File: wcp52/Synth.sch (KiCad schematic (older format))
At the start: 52 parts, among them U3 LMH6714MF, U4 AD9958BCPZ, U5 LMH6714MF, X1 25 MHz

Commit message: Reorganize MPU schematic
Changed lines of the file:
@@
 Text HLabel 1350 4800 0    60   Input ~ 0
 SDI
-Text HLabel 1350 4900 0    60   Input ~ 0
+Text HLabel 1350 4900 0    60   BiDi ~ 0
 SDIO_1
 Text HLabel 1350 5000 0    60   Output ~ 0

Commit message: Reannotate parts. May need to tweak silkscreen
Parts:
- C10: renamed from C6; OldReference (none) -> C6
- C11: renamed from C14; OldReference (none) -> C14
- C12: renamed from C7; OldReference (none) -> C7
- C13: renamed from C15; OldReference (none) -> C15
- C14: renamed from C11; OldReference (none) -> C11
- C15: renamed from C12; OldReference (none) -> C12
- C16: renamed from C8; OldReference (none) -> C8
- C17: renamed from C16; OldReference (none) -> C16
- C18: renamed from C9; OldReference (none) -> C9
- C19: renamed from C17; OldReference (none) -> C17
- C20: renamed from C10; OldReference (none) -> C10
- C21: renamed from C19; OldReference (none) -> C19
- C22: renamed from C20; OldReference (none) -> C20
- C23: renamed from C21; OldReference (none) -> C21
- C24: renamed from C22; OldReference (none) -> C22
- C25: renamed from C23; OldReference (none) -> C23
- C26: renamed from C24; OldReference (none) -> C24
- C27: renamed from C25; OldReference (none) -> C25
- C28: renamed from C26; OldReference (none) -> C26
- C29: renamed from C27; OldReference (none) -> C27
- C30: renamed from C18; OldReference (none) -> C18
- C31: renamed from C55; OldReference (none) -> C55
- C8: renamed from C5; OldReference (none) -> C5
- C9: renamed from C13; OldReference (none) -> C13
- E2: OldReference (none) -> E2
- R18: renamed from R13; OldReference (none) -> R13
- R19: renamed from R14; OldReference (none) -> R14
- R20: renamed from R12; OldReference (none) -> R12
- R21: renamed from R15; OldReference (none) -> R15
- R22: renamed from R17; OldReference (none) -> R17
- R23: renamed from R18; OldReference (none) -> R18
- R24: renamed from R19; OldReference (none) -> R19
- R25: renamed from R20; OldReference (none) -> R20
- R26: renamed from R21; OldReference (none) -> R21
- R27: renamed from R22; OldReference (none) -> R22
- R28: renamed from R23; OldReference (none) -> R23
- R29: renamed from R24; OldReference (none) -> R24
- R30: renamed from R25; OldReference (none) -> R25
- R31: renamed from R26; OldReference (none) -> R26
- R32: renamed from R27; OldReference (none) -> R27
- R33: renamed from R28; OldReference (none) -> R28
- R34: renamed from R29; OldReference (none) -> R29
- R35: renamed from R30; OldReference (none) -> R30
- R36: renamed from R31; OldReference (none) -> R31
- R37: renamed from R32; OldReference (none) -> R32
- R38: renamed from R33; OldReference (none) -> R33
- R39: renamed from R34; OldReference (none) -> R34
- TP6: renamed from TP2; OldReference (none) -> TP2
- U2: renamed from U3; OldReference (none) -> U3
- U3: renamed from U4; OldReference (none) -> U4
- U4: renamed from U5; OldReference (none) -> U5
- X1: OldReference (none) -> X1
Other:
- note added: "@R20 is copper-bridged on the PCB, it is not necessary to populate a jumper.\nIf this part must be changed after testing, cut the bridge."
- note removed: "@R12 is copper-bridged on the PCB, it is not necessary to populate a jumper.\nIf this part must be changed after testing, cut the bridge."

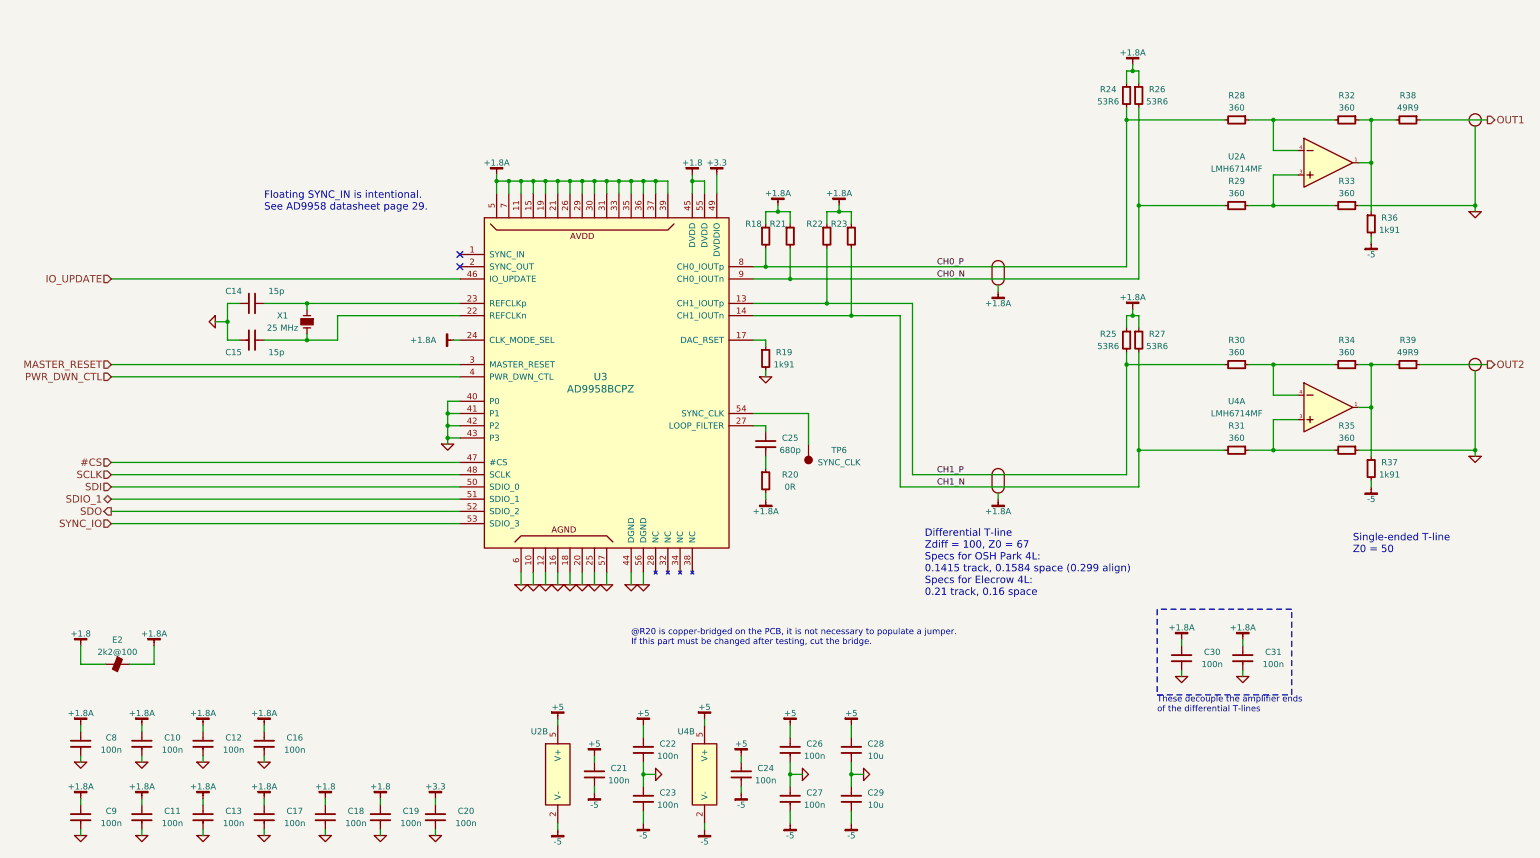
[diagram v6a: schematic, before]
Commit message: Change schematic pages to letter size
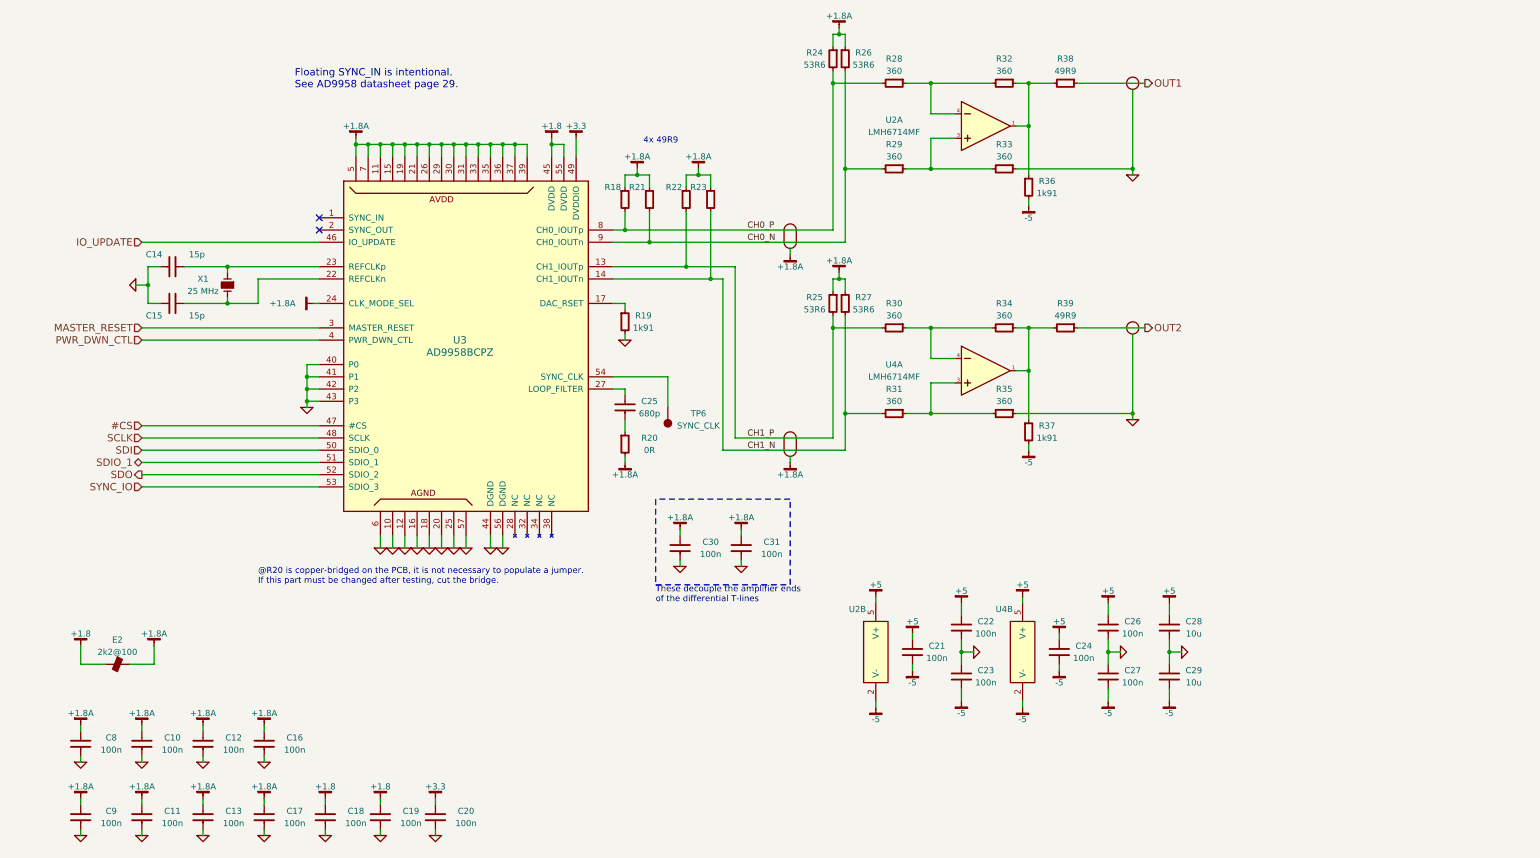
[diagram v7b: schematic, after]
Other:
- note added: "4x 49R9"
- note removed: "Differential T-line\nZdiff = 100, Z0 = 67\nSpecs for OSH Park 4L:\n0.1415 track, 0.1584 space (0.299 align)\nSpecs for Elecrow 4L:\n0.21 track, 0.16 space"
- note removed: "Single-ended T-line\nZ0 = 50"
- moved on the sheet: C14, C15, C21, C22, C23, C24, C25, C26, C27, C28, C29, C30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

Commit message: BOM fixes
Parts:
- U2, U4: BOM DIST DIGIKEY LMH6714MF/NOPBCT-ND -> IC TI LMH6714MF
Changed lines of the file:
@@
 EESchema Schematic File Version 2
-LIBS:Altera
-LIBS:AnalogDevices
-LIBS:Atmel
-LIBS:conn-2mm
-LIBS:conn-100mil
-LIBS:conn-cui
-LIBS:conn-fci
-LIBS:conn-linx
-LIBS:conn-molex
-LIBS:conn-tagconnect
-LIBS:conn-test
-LIBS:DiodesInc
-LIBS:display
-LIBS:_electromech
-LIBS:Fairchild
-LIBS:FTDI
-LIBS:Intersil
-LIBS:Lattice
-LIBS:_linear
-LIBS:LinearTech
-LIBS:Littelfuse
-LIBS:logic-4000
-LIBS:logic-7400
-LIBS:MACOM
-LIBS:maxim
-LIBS:mechanical
-LIBS:Microchip
-LIBS:Micron
-LIBS:NXP
-LIBS:onsemi
-LIBS:passive
-LIBS:pasv-BiTech
-LIBS:pasv-Bourns
-LIBS:pasv-cap
-LIBS:pasv-ind
-LIBS:pasv-res
-LIBS:pcb
-LIBS:power
-LIBS:_semi
-LIBS:semi-diode-1N
-LIBS:semi-diode-BA
-LIBS:semi-diode-MCC
-LIBS:semi-diode-MMB
-LIBS:semi-diode-NXP
-LIBS:semi-diode-OnSemi
-LIBS:semi-diode-Vishay
-LIBS:semi-opto-misc
-LIBS:semi-thyristor-2N
-LIBS:semi-trans-2N
-LIBS:semi-trans-AO
-LIBS:semi-trans-BC
-LIBS:semi-trans-DiodesInc
-LIBS:semi-trans-Fairchild
-LIBS:semi-trans-Infineon
-LIBS:semi-trans-IntRect
-LIBS:semi-trans-IXYS
-LIBS:semi-trans-misc
-LIBS:semi-trans-MMB
-LIBS:semi-trans-MPS
-LIBS:semi-trans-NXP
-LIBS:semi-trans-PZT
-LIBS:semi-trans-TI
-LIBS:semi-trans-TIP
-LIBS:semi-trans-Toshiba
-LIBS:silabs
-LIBS:skyworks
-LIBS:ST
-LIBS:st_ic
-LIBS:st_semi
-LIBS:supertex
-LIBS:symbol
-LIBS:TexasInstruments
-LIBS:vishay_semi
-LIBS:Xilinx
-LIBS:pasv-xtal
-LIBS:conn-te
 LIBS:wcp52-cache
 EELAYER 25 0
@@
 F 2 "smd-semi:SOT-23-5" H 8500 1850 50  0001 C CNN
 F 3 "" H 8300 1850 60  0000 C CNN
-F 4 "DIST DIGIKEY LMH6714MF/NOPBCT-ND" H 9000 2700 60  0001 C CNN "BOM"
-F 5 "Value" H 8500 1850 60  0001 C CNN "Manuf"
+F 4 "Value" H 8500 1850 60  0001 C CNN "Manuf"
+F 5 "IC TI LMH6714MF" H 9000 2700 60  0001 C CNN "BOM"
 F 6 "U3" H 8500 1850 50  0001 C CNN "OldReference"
 	1    8500 1850
@@
 F 2 "smd-semi:SOT-23-5" H 8500 3850 50  0001 C CNN
 F 3 "" H 8300 3850 60  0000 C CNN
-F 4 "DIST DIGIKEY LMH6714MF/NOPBCT-ND" H 9000 4700 60  0001 C CNN "BOM"
-F 5 "Value" H 8500 3850 60  0001 C CNN "Manuf"
+F 4 "Value" H 8500 3850 60  0001 C CNN "Manuf"
+F 5 "IC TI LMH6714MF" H 9000 4700 60  0001 C CNN "BOM"
 F 6 "U5" H 8500 3850 50  0001 C CNN "OldReference"
 	1    8500 3850
